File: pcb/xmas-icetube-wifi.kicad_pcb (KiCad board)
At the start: 2 copper layers, 35.4 x 18.4 mm, 18 parts, among them J1 Conn_01x03, J2 Conn_01x06, SW1 SW_SPDT, SW2 SW_Push, SW3 SW_Push, U1 AP2112K-3.3, U2 74AHCT1G125, U3 ESP-M3

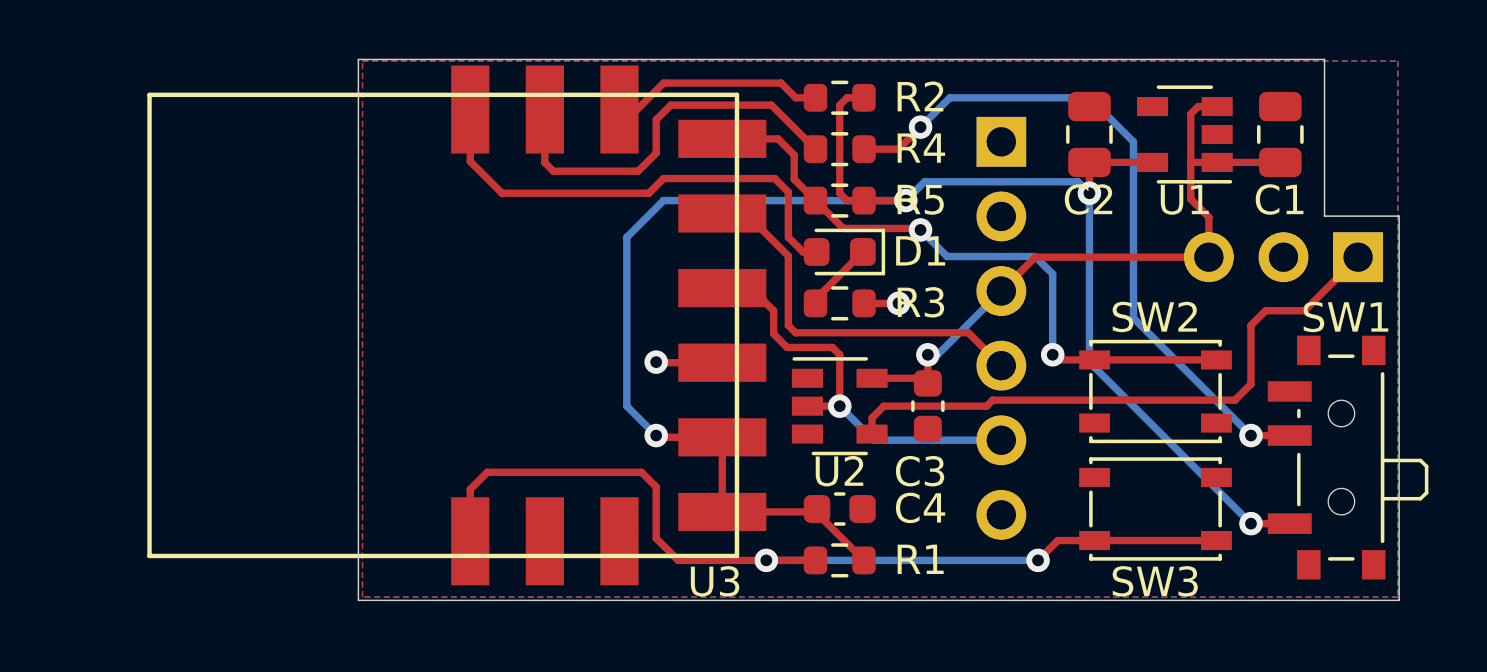
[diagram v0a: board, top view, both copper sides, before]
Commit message: Updating PCB with longer ESP-M3 footprint
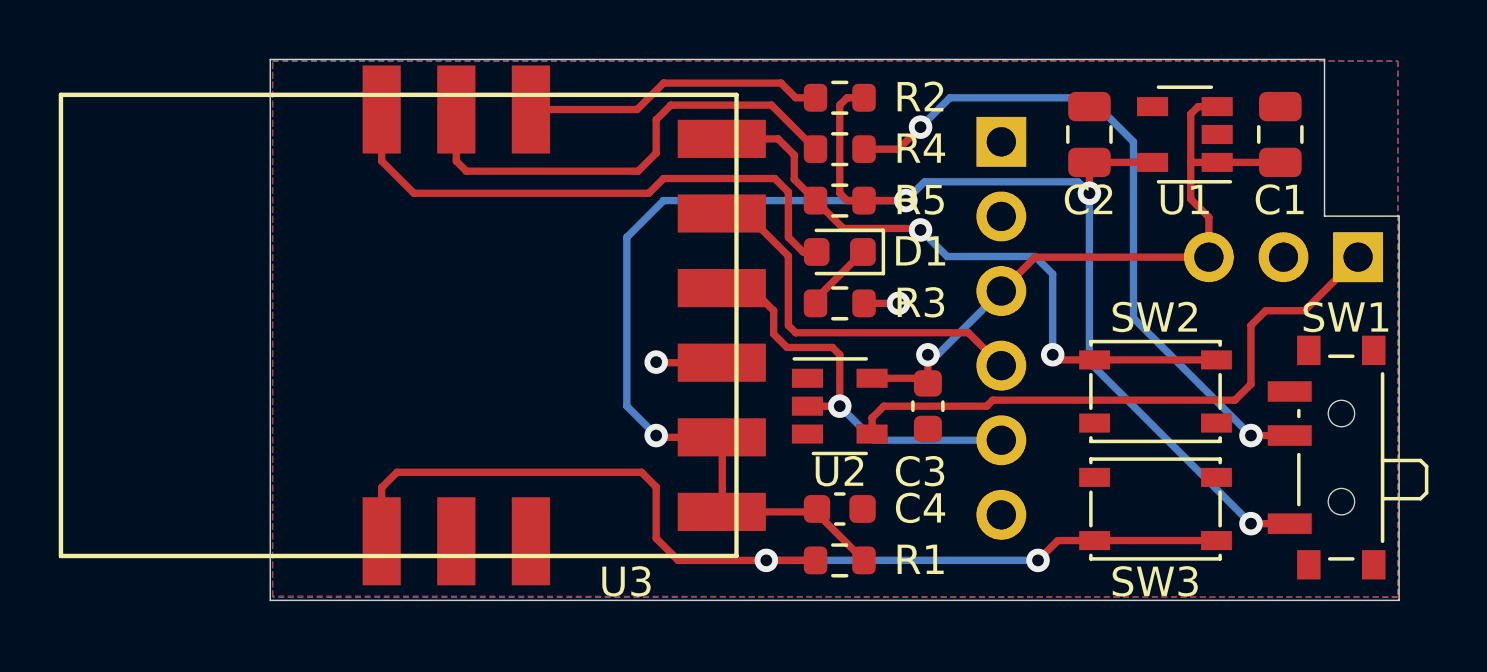
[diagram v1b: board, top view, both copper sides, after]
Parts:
- moved U3 3.02 mm to (30.7, -10.2)
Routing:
- net /BUTTON: track 31.6 -> 34.7 mm
- net Net-(R2-Pad1): track 7.25 -> 10.3 mm
- net Net-(D1-Pad2): track 16.2 -> 19.2 mm
- net Net-(R4-Pad1): track 13.4 -> 16.3 mm
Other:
- board size 35.4 x 18.4 mm -> 38.4 x 18.4 mm
